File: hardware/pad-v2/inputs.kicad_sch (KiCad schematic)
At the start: 27 parts, among them J301 Toggle PERSONAL-OFF-WORK, SW301 MX switch (hot-swap socket), SW302 MX switch (hot-swap socket), SW303 MX switch (hot-swap socket), SW304 MX switch (hot-swap socket), SW305 MX switch (hot-swap socket), SW306 MX switch (hot-swap socket), SW307 MX switch (hot-swap socket), SW308 MX switch (hot-swap socket), SW309 MX switch (hot-swap socket), SW310 MX switch (hot-swap socket), SW311 MX switch (hot-swap socket), SW312 MX switch (hot-swap socket), SW313 PEC11R-4220F-S0024, SW314 PEC11R-4220F-S0024

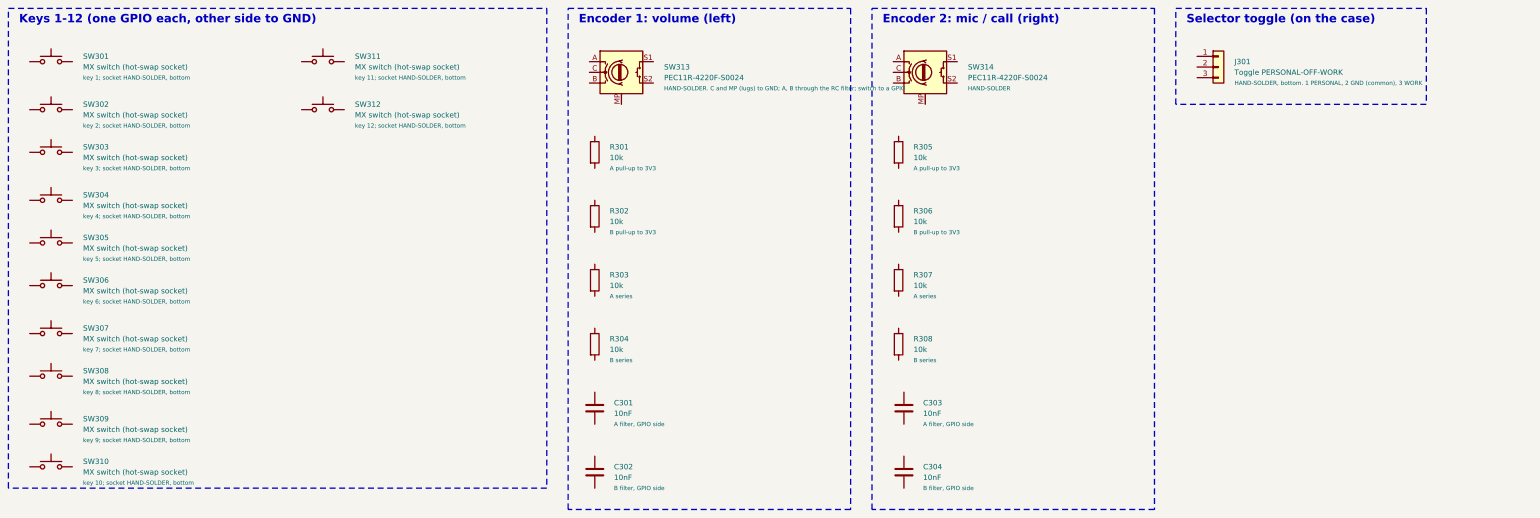
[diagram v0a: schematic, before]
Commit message: Pad v2: GPIO map for routing, PAD_WIRING.md (component-by-component), connection model + checker; battery 2-pin + NTC header, USB-C to the front edge, LED chain starts at key 9
Co-Authored-By: Claude Opus 5.5 <noreply@anthropic.com>
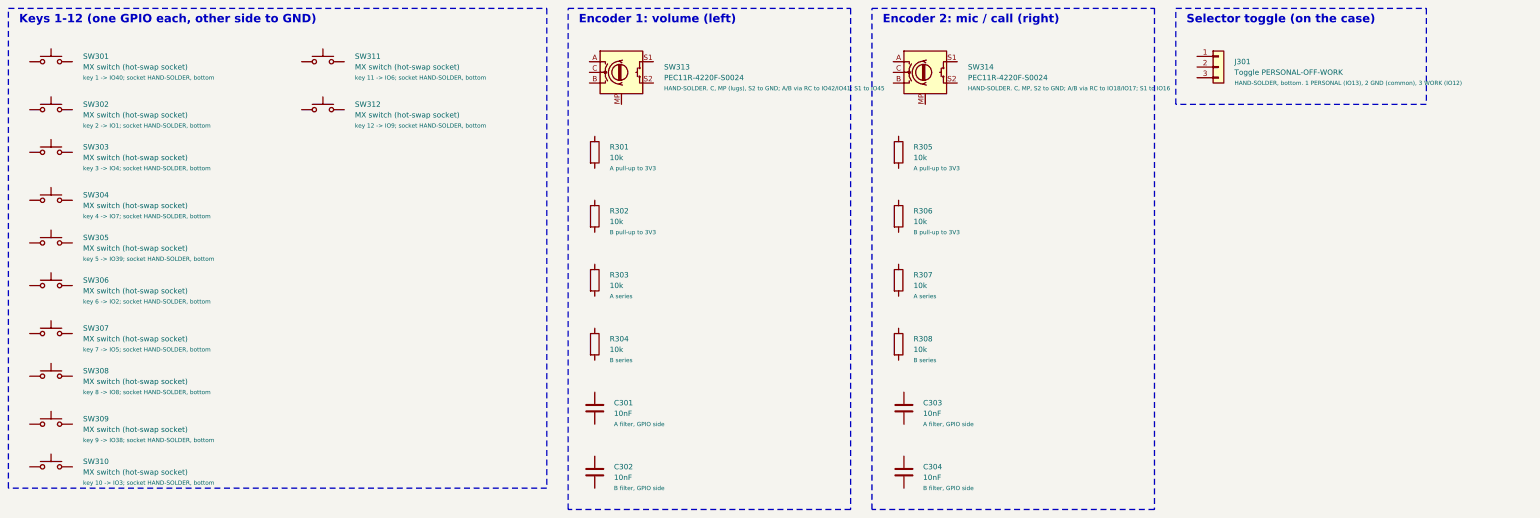
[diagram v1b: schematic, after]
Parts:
- J301: Note HAND-SOLDER, bottom. 1 PERSONAL, 2 GND (common), 3 WORK -> HAND-SOLDER, bottom. 1 PERSONAL (IO13), 2 GND (common), 3 W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
- SW301: Note key 1; socket HAND-SOLDER, bottom -> key 1 -> IO40; socket HAND-SOLDER, bottom
- SW302: Note key 2; socket HAND-SOLDER, bottom -> key 2 -> IO1; socket HAND-SOLDER, bottom
- SW303: Note key 3; socket HAND-SOLDER, bottom -> key 3 -> IO4; socket HAND-SOLDER, bottom
- SW304: Note key 4; socket HAND-SOLDER, bottom -> key 4 -> IO7; socket HAND-SOLDER, bottom
- SW305: Note key 5; socket HAND-SOLDER, bottom -> key 5 -> IO39; socket HAND-SOLDER, bottom
- SW306: Note key 6; socket HAND-SOLDER, bottom -> key 6 -> IO2; socket HAND-SOLDER, bottom
- SW307: Note key 7; socket HAND-SOLDER, bottom -> key 7 -> IO5; socket HAND-SOLDER, bottom
- SW308: Note key 8; socket HAND-SOLDER, bottom -> key 8 -> IO8; socket HAND-SOLDER, bottom
- SW309: Note key 9; socket HAND-SOLDER, bottom -> key 9 -> IO38; socket HAND-SOLDER, bottom
- SW310: Note key 10; socket HAND-SOLDER, bottom -> key 10 -> IO3; socket HAND-SOLDER, bottom
- SW311: Note key 11; socket HAND-SOLDER, bottom -> key 11 -> IO6; socket HAND-SOLDER, bottom
- SW312: Note key 12; socket HAND-SOLDER, bottom -> key 12 -> IO9; socket HAND-SOLDER, bottom
- SW313: Note HAND-SOLDER. C and MP (lugs) to GND; A, B through the RC fi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 -> HAND-SOLDER. C, MP (lugs), S2 to GND; A/B via RC to IO42/IO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
- SW314: Note HAND-SOLDER -> HAND-SOLDER. C, MP, S2 to GND; A/B via RC to IO18/IO17; S1 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
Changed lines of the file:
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@@
 			)
 		)
-		(property "Note" "key 1; socket HAND-SOLDER, bottom"
+		(property "Note" "key 1 -> IO40; socket HAND-SOLDER, bottom"
 			(at 30.48 34.29 0)
 			(show_name no)
@@
 		(instances
 			(project "pad-v2"
-				(path "/c348787c-35a6-4c40-81d7-0eeb948bfe4d/3728a1c4-dc90-4859-af3f-dfb5c2605473"
+				(path "/aa63e03b-1ac8-4926-b623-c7b31956768e/9f788691-5465-4206-8a9a-b890c56a605e"
 					(reference "SW301")
 					(unit 1)
@@
 			)
 		)
-		(property "Note" "key 2; socket HAND-SOLDER, bottom"
+		(property "Note" "key 2 -> IO1; socket HAND-SOLDER, bottom"
 			(at 30.48 45.72 0)
 			(show_name no)
@@
 		(instances
 			(project "pad-v2"
-				(path "/c348787c-35a6-4c40-81d7-0eeb948bfe4d/3728a1c4-dc90-4859-af3f-dfb5c2605473"
+				(path "/aa63e03b-1ac8-4926-b623-c7b31956768e/9f788691-5465-4206-8a9a-b890c56a605e"
 					(reference "SW302")
 					(unit 1)
@@
 			)
 		)
-		(property "Note" "key 3; socket HAND-SOLDER, bottom"
+		(property "Note" "key 3 -> IO4; socket HAND-SOLDER, bottom"
 			(at 30.48 55.88 0)
 			(show_name no)
@@
 		(instances
 			(project "pad-v2"
-				(path "/c348787c-35a6-4c40-81d7-0eeb948bfe4d/3728a1c4-dc90-4859-af3f-dfb5c2605473"
+				(path "/aa63e03b-1ac8-4926-b623-c7b31956768e/9f788691-5465-4206-8a9a-b890c56a605e"
 					(reference "SW303")
 					(unit 1)
@@
 			)
 		)
-		(property "Note" "key 4; socket HAND-SOLDER, bottom"
+		(property "Note" "key 4 -> IO7; socket HAND-SOLDER, bottom"
 			(at 30.48 67.31 0)
 			(show_name no)
@@
 		(instances
 			(project "pad-v2"
-				(path "/c348787c-35a6-4c40-81d7-0eeb948bfe4d/3728a1c4-dc90-4859-af3f-dfb5c2605473"
+				(path "/aa63e03b-1ac8-4926-b623-c7b31956768e/9f788691-5465-4206-8a9a-b890c56a605e"
 					(reference "SW304")
 					(unit 1)
@@
 			)
 		)
-		(property "Note" "key 5; socket HAND-SOLDER, bottom"
+		(property "Note" "key 5 -> IO39; socket HAND-SOLDER, bottom"
 			(at 30.48 77.47 0)
 			(show_name no)
@@
 		(instances
 			(project "pad-v2"
-				(path "/c348787c-35a6-4c40-81d7-0eeb948bfe4d/3728a1c4-dc90-4859-af3f-dfb5c2605473"
+				(path "/aa63e03b-1ac8-4926-b623-c7b31956768e/9f788691-5465-4206-8a9a-b890c56a605e"
 					(reference "SW305")
 					(unit 1)
@@
 			)
 		)
-		(property "Note" "key 6; socket HAND-SOLDER, bottom"
+		(property "Note" "key 6 -> IO2; socket HAND-SOLDER, bottom"
 			(at 30.48 87.63 0)
 			(show_name no)
@@
 		(instances
 			(project "pad-v2"
-				(path "/c348787c-35a6-4c40-81d7-0eeb948bfe4d/3728a1c4-dc90-4859-af3f-dfb5c2605473"
+				(path "/aa63e03b-1ac8-4926-b623-c7b31956768e/9f788691-5465-4206-8a9a-b890c56a605e"
 					(reference "SW306")
 					(unit 1)
@@
 			)
 		)
-		(property "Note" "key 7; socket HAND-SOLDER, bottom"
+		(property "Note" "key 7 -> IO5; socket HAND-SOLDER, bottom"
 			(at 30.48 99.06 0)
 			(show_name no)
@@
 		(instances
 			(project "pad-v2"
-				(path "/c348787c-35a6-4c40-81d7-0eeb948bfe4d/3728a1c4-dc90-4859-af3f-dfb5c2605473"
+				(path "/aa63e03b-1ac8-4926-b623-c7b31956768e/9f788691-5465-4206-8a9a-b890c56a605e"
 					(reference "SW307")
 					(unit 1)
@@
 			)
 		)
-		(property "Note" "key 8; socket HAND-SOLDER, bottom"
+		(property "Note" "key 8 -> IO8; socket HAND-SOLDER, bottom"
 			(at 30.48 109.22 0)
 			(show_name no)
@@
 		(instances
 			(project "pad-v2"
-				(path "/c348787c-35a6-4c40-81d7-0eeb948bfe4d/3728a1c4-dc90-4859-af3f-dfb5c2605473"
+				(path "/aa63e03b-1ac8-4926-b623-c7b31956768e/9f788691-5465-4206-8a9a-b890c56a605e"
 					(reference "SW308")
 					(unit 1)
@@
 			)
 		)
-		(property "Note" "key 9; socket HAND-SOLDER, bottom"
+		(property "Note" "key 9 -> IO38; socket HAND-SOLDER, bottom"
 			(at 30.48 120.65 0)
 			(show_name no)
@@
 		(instances
 			(project "pad-v2"
-				(path "/c348787c-35a6-4c40-81d7-0eeb948bfe4d/3728a1c4-dc90-4859-af3f-dfb5c2605473"
+				(path "/aa63e03b-1ac8-4926-b623-c7b31956768e/9f788691-5465-4206-8a9a-b890c56a605e"
 					(reference "SW309")
 					(unit 1)
@@
 			)
 		)
-		(property "Note" "key 10; socket HAND-SOLDER, bottom"
+		(property "Note" "key 10 -> IO3; socket HAND-SOLDER, bottom"
 			(at 30.48 130.81 0)
 			(show_name no)
@@
 		(instances
 			(project "pad-v2"
-				(path "/c348787c-35a6-4c40-81d7-0eeb948bfe4d/3728a1c4-dc90-4859-af3f-dfb5c2605473"
+				(path "/aa63e03b-1ac8-4926-b623-c7b31956768e/9f788691-5465-4206-8a9a-b890c56a605e"
 					(reference "SW310")
 					(unit 1)
@@
 			)
 		)
-		(property "Note" "key 11; socket HAND-SOLDER, bottom"
+		(property "Note" "key 11 -> IO6; socket HAND-SOLDER, bottom"
 			(at 95.25 34.29 0)
 			(show_name no)
@@
 		(instances
 			(project "pad-v2"
-				(path "/c348787c-35a6-4c40-81d7-0eeb948bfe4d/3728a1c4-dc90-4859-af3f-dfb5c2605473"
+				(path "/aa63e03b-1ac8-4926-b623-c7b31956768e/9f788691-5465-4206-8a9a-b890c56a605e"
 					(reference "SW311")
 					(unit 1)
@@
 			)
 		)
-		(property "Note" "key 12; socket HAND-SOLDER, bottom"
+		(property "Note" "key 12 -> IO9; socket HAND-SOLDER, bottom"
 			(at 95.25 45.72 0)
 			(show_name no)
@@
 		(instances
 			(project "pad-v2"
-				(path "/c348787c-35a6-4c40-81d7-0eeb948bfe4d/3728a1c4-dc90-4859-af3f-dfb5c2605473"
+				(path "/aa63e03b-1ac8-4926-b623-c7b31956768e/9f788691-5465-4206-8a9a-b890c56a605e"
 					(reference "SW312")
 					(unit 1)
@@
 			)
 		)
-		(property "Note" "HAND-SOLDER. C and MP (lugs) to GND; A, B through the RC filter; switch to a GPIO"
+		(property "Note" "HAND-SOLDER. C, MP (lugs), S2 to GND; A/B via RC to IO42/IO41; S1 to IO45"
 			(at 168.91 36.83 0)
 			(show_name no)
@@
 		(instances
 			(project "pad-v2"
-				(path "/c348787c-35a6-4c40-81d7-0eeb948bfe4d/3728a1c4-dc90-4859-af3f-dfb5c2605473"
+				(path "/aa63e03b-1ac8-4926-b623-c7b31956768e/9f788691-5465-4206-8a9a-b890c56a605e"
 					(reference "SW313")
 					(unit 1)
@@
 		(instances
 			(project "pad-v2"
-				(path "/c348787c-35a6-4c40-81d7-0eeb948bfe4d/3728a1c4-dc90-4859-af3f-dfb5c2605473"
+				(path "/aa63e03b-1ac8-4926-b623-c7b31956768e/9f788691-5465-4206-8a9a-b890c56a605e"
 					(reference "R301")
 					(unit 1)
@@
 		(instances
 			(project "pad-v2"
-				(path "/c348787c-35a6-4c40-81d7-0eeb948bfe4d/3728a1c4-dc90-4859-af3f-dfb5c2605473"
+				(path "/aa63e03b-1ac8-4926-b623-c7b31956768e/9f788691-5465-4206-8a9a-b890c56a605e"
 					(reference "R302")
 					(unit 1)
@@
 		(instances
 			(project "pad-v2"
-				(path "/c348787c-35a6-4c40-81d7-0eeb948bfe4d/3728a1c4-dc90-4859-af3f-dfb5c2605473"
+				(path "/aa63e03b-1ac8-4926-b623-c7b31956768e/9f788691-5465-4206-8a9a-b890c56a605e"
 					(reference "R303")
 					(unit 1)
@@
 		(instances
 			(project "pad-v2"
-				(path "/c348787c-35a6-4c40-81d7-0eeb948bfe4d/3728a1c4-dc90-4859-af3f-dfb5c2605473"
+				(path "/aa63e03b-1ac8-4926-b623-c7b31956768e/9f788691-5465-4206-8a9a-b890c56a605e"
 					(reference "R304")
 					(unit 1)
@@
 		(instances
 			(project "pad-v2"
-				(path "/c348787c-35a6-4c40-81d7-0eeb948bfe4d/3728a1c4-dc90-4859-af3f-dfb5c2605473"
+				(path "/aa63e03b-1ac8-4926-b623-c7b31956768e/9f788691-5465-4206-8a9a-b890c56a605e"
 					(reference "C301")
 					(unit 1)
@@
 		(instances
 			(project "pad-v2"
-				(path "/c348787c-35a6-4c40-81d7-0eeb948bfe4d/3728a1c4-dc90-4859-af3f-dfb5c2605473"
+				(path "/aa63e03b-1ac8-4926-b623-c7b31956768e/9f788691-5465-4206-8a9a-b890c56a605e"
 					(reference "C302")
 					(unit 1)
@@
 			)
 		)
-		(property "Note" "HAND-SOLDER"
+		(property "Note" "HAND-SOLDER. C, MP, S2 to GND; A/B via RC to IO18/IO17; S1 to IO16"
 			(at 241.30 36.83 0)
 			(show_name no)
@@
 		(instances
 			(project "pad-v2"
-				(path "/c348787c-35a6-4c40-81d7-0eeb948bfe4d/3728a1c4-dc90-4859-af3f-dfb5c2605473"
+				(path "/aa63e03b-1ac8-4926-b623-c7b31956768e/9f788691-5465-4206-8a9a-b890c56a605e"
 					(reference "SW314")
 					(unit 1)
@@
 		(instances
 			(project "pad-v2"
-				(path "/c348787c-35a6-4c40-81d7-0eeb948bfe4d/3728a1c4-dc90-4859-af3f-dfb5c2605473"
+				(path "/aa63e03b-1ac8-4926-b623-c7b31956768e/9f788691-5465-4206-8a9a-b890c56a605e"
 					(reference "R305")
 					(unit 1)
@@
 		(instances
 			(project "pad-v2"
-				(path "/c348787c-35a6-4c40-81d7-0eeb948bfe4d/3728a1c4-dc90-4859-af3f-dfb5c2605473"
+				(path "/aa63e03b-1ac8-4926-b623-c7b31956768e/9f788691-5465-4206-8a9a-b890c56a605e"
 					(reference "R306")
 					(unit 1)
@@
 		(instances
 			(project "pad-v2"
-				(path "/c348787c-35a6-4c40-81d7-0eeb948bfe4d/3728a1c4-dc90-4859-af3f-dfb5c2605473"
+				(path "/aa63e03b-1ac8-4926-b623-c7b31956768e/9f788691-5465-4206-8a9a-b890c56a605e"
 					(reference "R307")
 					(unit 1)
@@
 		(instances
 			(project "pad-v2"
-				(path "/c348787c-35a6-4c40-81d7-0eeb948bfe4d/3728a1c4-dc90-4859-af3f-dfb5c2605473"
+				(path "/aa63e03b-1ac8-4926-b623-c7b31956768e/9f788691-5465-4206-8a9a-b890c56a605e"
 					(reference "R308")
 					(unit 1)
@@
 		(instances
 			(project "pad-v2"
-				(path "/c348787c-35a6-4c40-81d7-0eeb948bfe4d/3728a1c4-dc90-4859-af3f-dfb5c2605473"
+				(path "/aa63e03b-1ac8-4926-b623-c7b31956768e/9f788691-5465-4206-8a9a-b890c56a605e"
 					(reference "C303")
 					(unit 1)
@@
 		(instances
 			(project "pad-v2"
-				(path "/c348787c-35a6-4c40-81d7-0eeb948bfe4d/3728a1c4-dc90-4859-af3f-dfb5c2605473"
+				(path "/aa63e03b-1ac8-4926-b623-c7b31956768e/9f788691-5465-4206-8a9a-b890c56a605e"
 					(reference "C304")
 					(unit 1)
@@
 			)
 		)
-		(property "Note" "HAND-SOLDER, bottom. 1 PERSONAL, 2 GND (common), 3 WORK"
+		(property "Note" "HAND-SOLDER, bottom. 1 PERSONAL (IO13), 2 GND (common), 3 WORK (IO12)"
 			(at 304.80 35.56 0)
 			(show_name no)
@@
 		(instances
 			(project "pad-v2"
-				(path "/c348787c-35a6-4c40-81d7-0eeb948bfe4d/3728a1c4-dc90-4859-af3f-dfb5c2605473"
+				(path "/aa63e03b-1ac8-4926-b623-c7b31956768e/9f788691-5465-4206-8a9a-b890c56a605e"
 					(reference "J301")
 					(unit 1)
